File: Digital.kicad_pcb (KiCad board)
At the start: 4 copper layers, 61 x 42 mm, 49 parts, among them J1 Conn_02x05_Odd_Even_MountingP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, Q1 Q_NMOS_GSD, U1 STM32F746VGTx, U2 MOUDLE-BLUETOOTH-HC-05(34P-27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, Y1 25MHz, Y2 32kHz

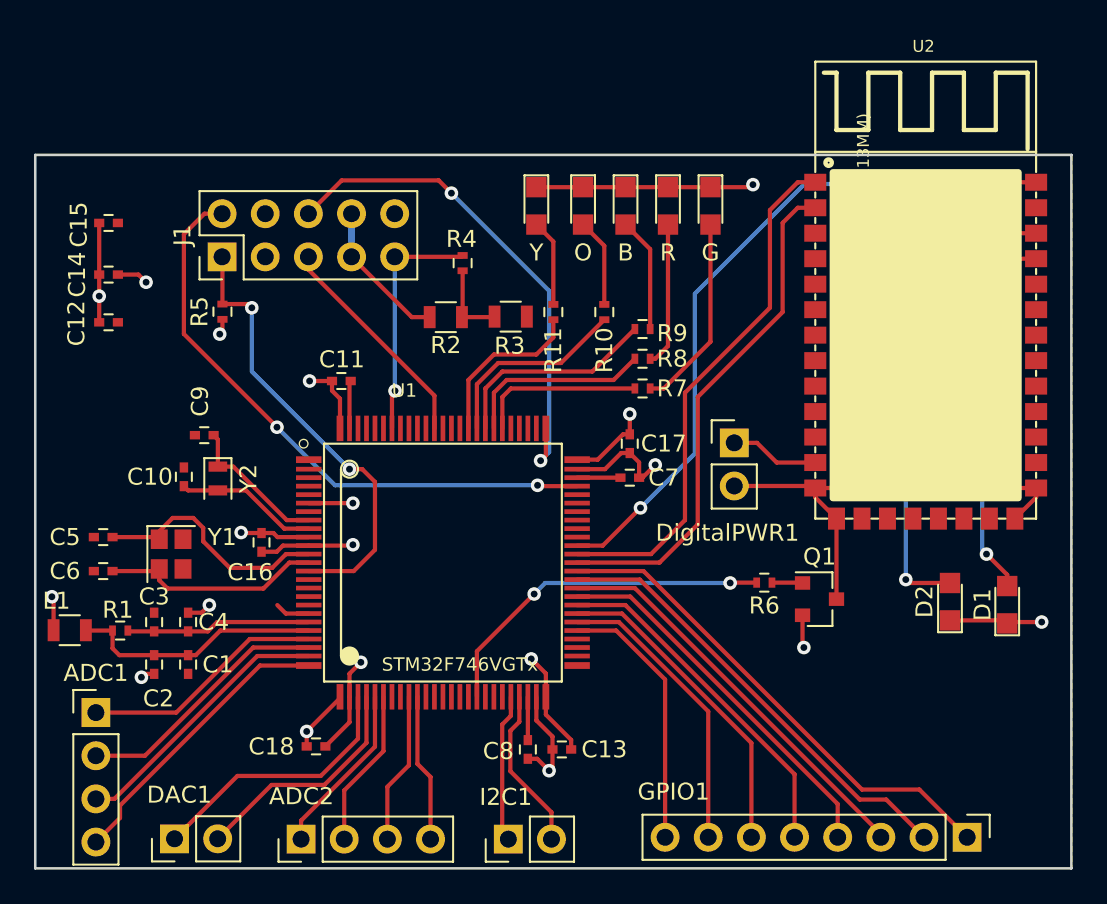
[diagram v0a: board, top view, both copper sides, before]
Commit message: Footprint changed in Y1
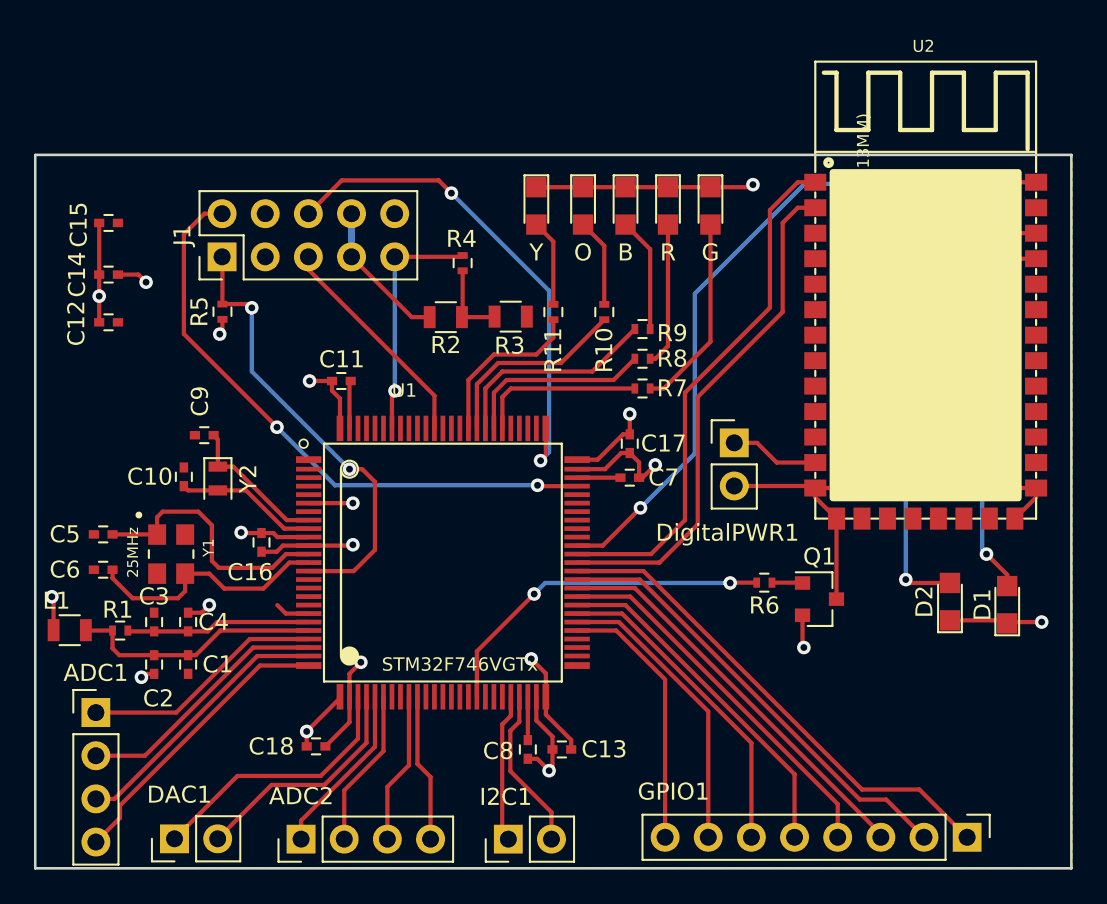
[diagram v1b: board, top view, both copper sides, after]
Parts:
- Y1: footprint Crystals:Crystal_SMD_2520-4pin_2.5x2.0mm -> User_library:OSCCC320X250X60N
- moved C5 0.16 mm to (134.0, 91.3)
- moved C6 0.08 mm to (134.0, 93.4)
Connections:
- Y1 pad 2: Net-(C6-Pad2) -> GND
- Y1 pad 3: (no net) -> Net-(C6-Pad2)
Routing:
- net Net-(C6-Pad2): track 13.1 -> 14.7 mm
- net Net-(C5-Pad2): track 14.4 -> 15.7 mm
